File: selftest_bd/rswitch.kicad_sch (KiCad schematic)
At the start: 105 parts, among them K1 TQ2-5_Split, K10 TQ2-5_Split, K11 TQ2-5_Split, K12 TQ2-5_Split, K13 TQ2-5_Split, K14 TQ2-5_Split, K15 TQ2-5_Split, K16 TQ2-5_Split, K17 TQ2-5_Split, K2 TQ2-5_Split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

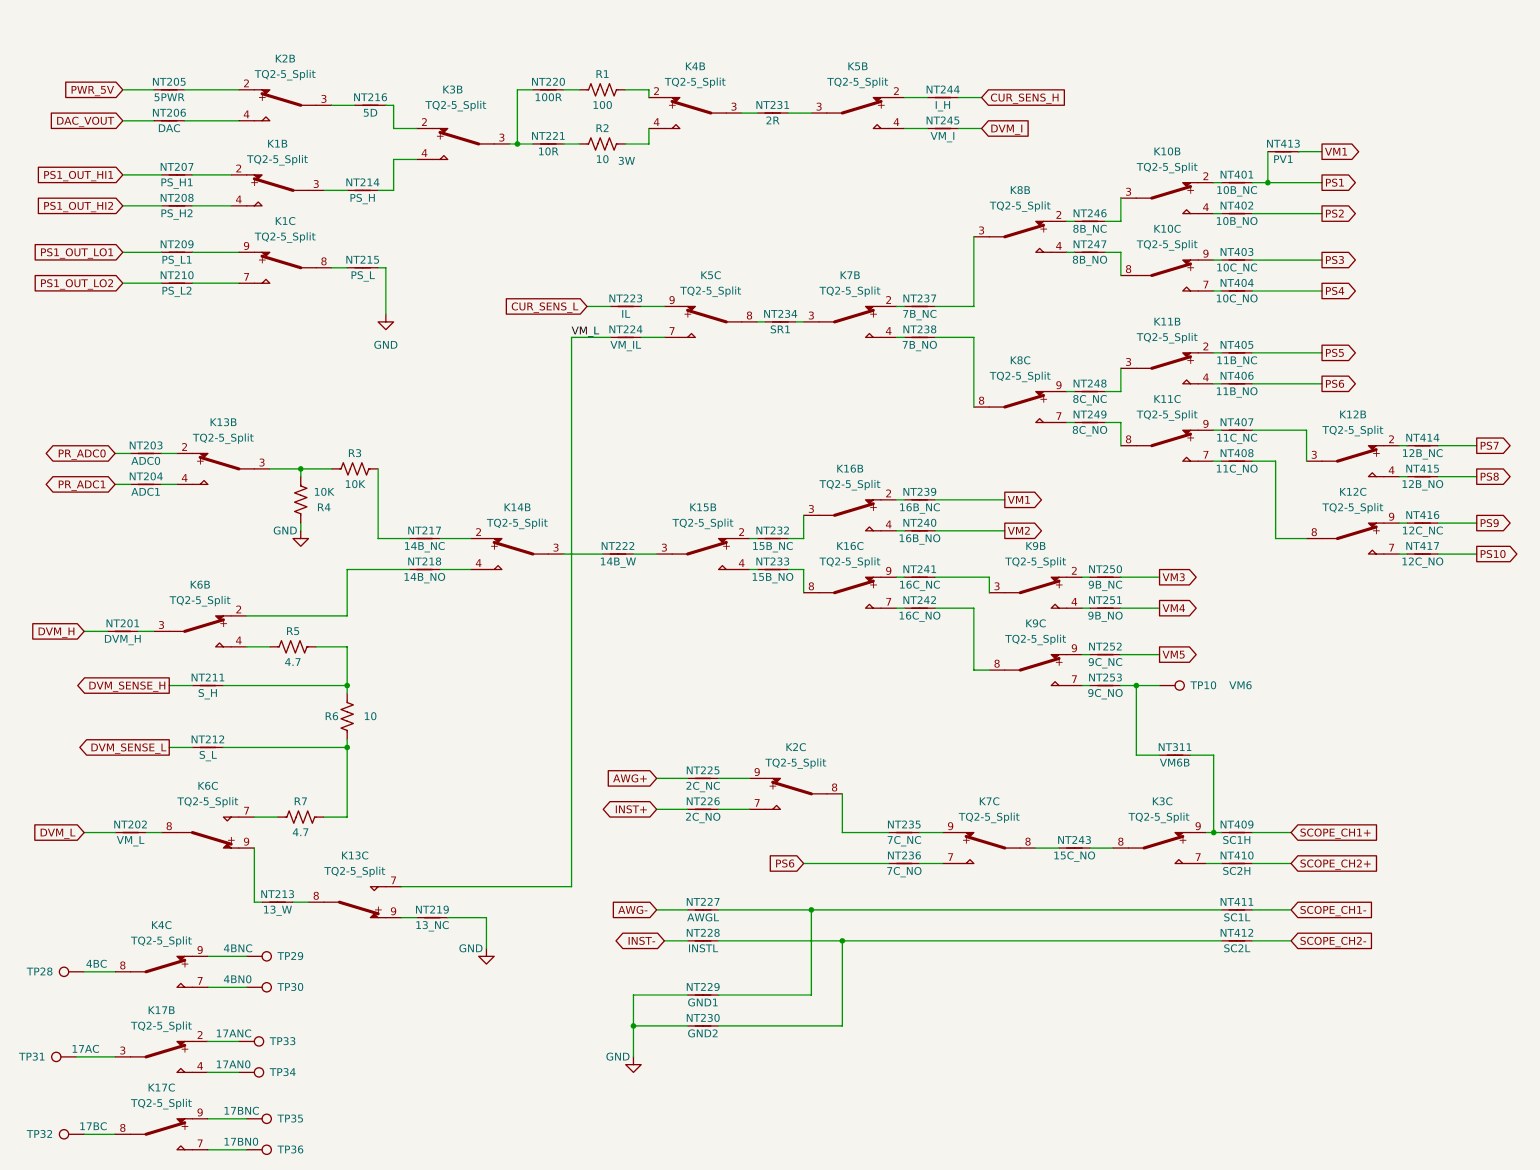
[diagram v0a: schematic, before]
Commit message: Commit V2.0
Redo PCB due to incorrect position of J1 and J2
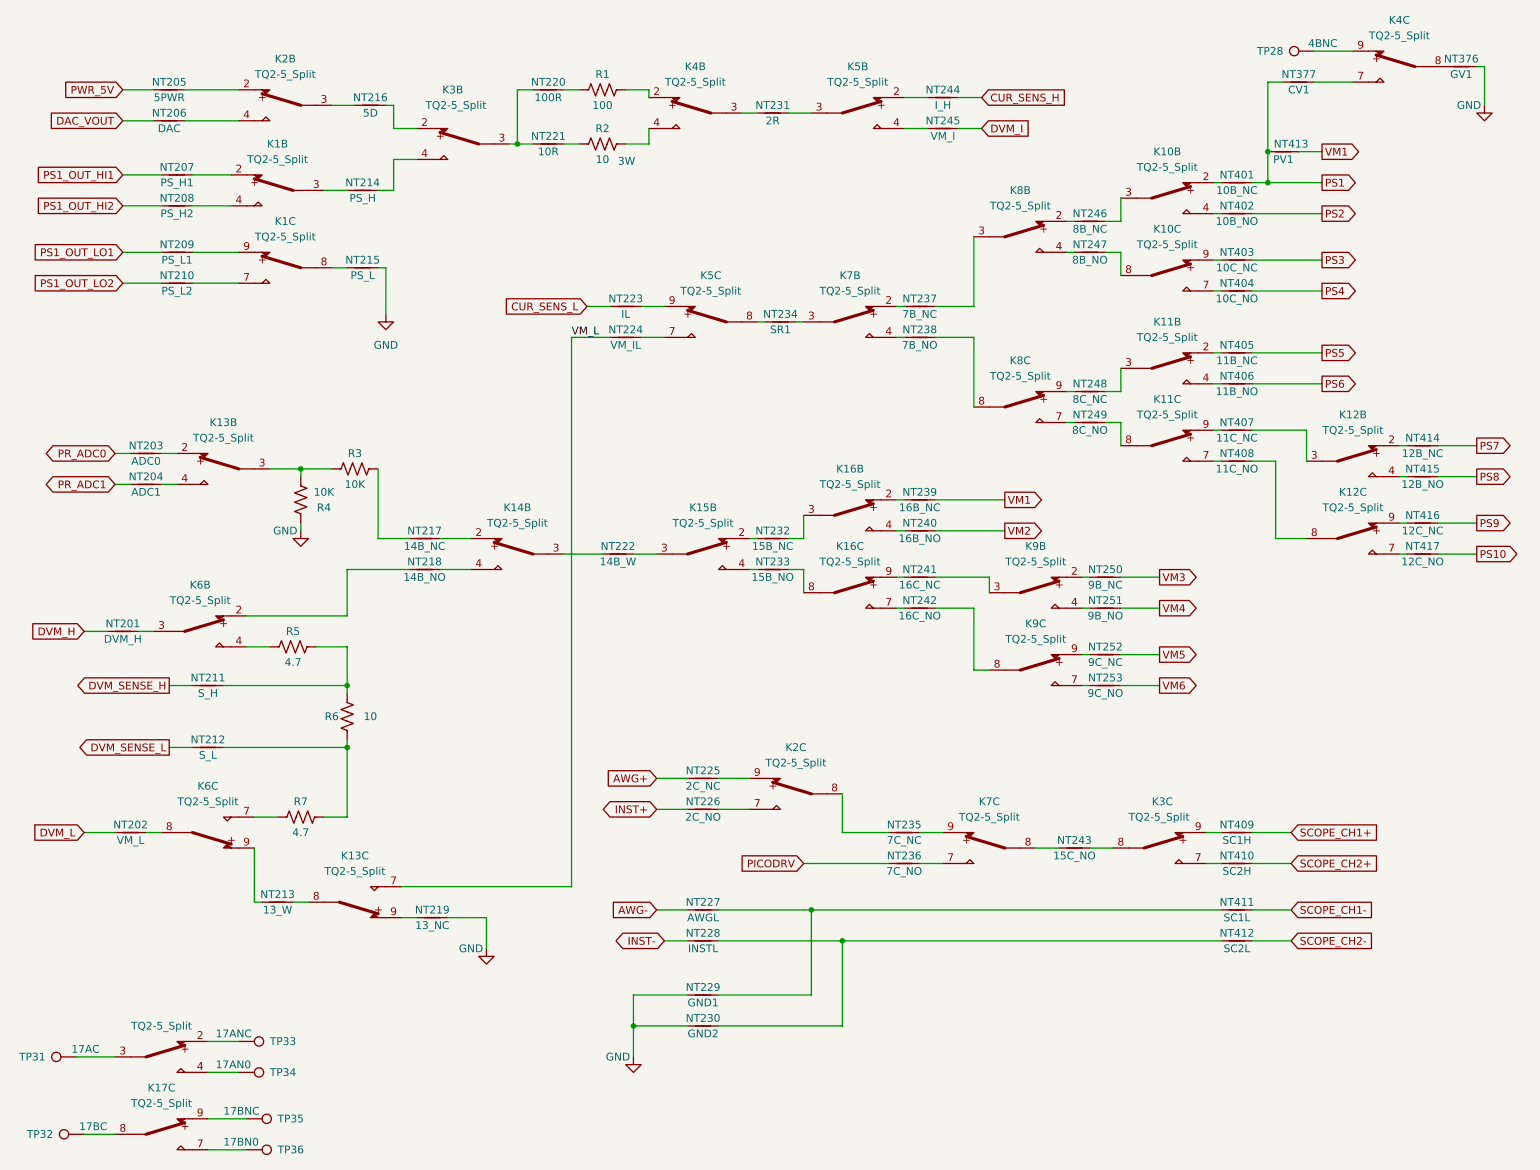
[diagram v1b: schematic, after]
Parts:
- removed NT311: VM6B, NetTie:NetTie-2_Front1.0mm, symbol Library:NetTie_2
- removed TP10: VM6, TestPoint:TestPoint_THTPad_D1.5mm_Drill0.7mm, symbol Library:TestPoint
- removed TP29: 4BNC, TestPoint:TestPoint_THTPad_D1.5mm_Drill0.7mm, symbol Library:TestPoint
- removed TP30: 4BN0, TestPoint:TestPoint_THTPad_D1.5mm_Drill0.7mm, symbol Library:TestPoint
- added NT376: GV1, NetTie:NetTie-2_Front1.0mm, symbol Library:NetTie_2
- added NT377: CV1, NetTie:NetTie-2_Front1.0mm, symbol Library:NetTie_2
- TP28: value 4BC -> 4BNC
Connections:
- net GND: now also NT376.2
- net PS1: now also NT377.1
- net PS6: no longer NT236.1
- net at K4.7: now also NT377.2
- net at K4.8: now also NT376.1; no longer TP28.1
- net at K4.9: now also TP28.1
- net VM6: now reaches NT253.2
- new net PICODRV: NT236.1
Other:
- title: FIRST TEST STATION SELFTEST BOARD 640-1010-010 -> FIRST TEST STATION SELFTEST BOARD 640-1010-020

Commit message: update README and small correction
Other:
- title: FIRST TEST STATION SELFTEST BOARD 640-1010-020 -> FIRST TEST STATION SELFTEST BOARD 640-1010-021
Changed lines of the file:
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@@
   (paper "A")
   (title_block
-    (title "FIRST TEST STATION SELFTEST BOARD 640-1010-020")
+    (title "FIRST TEST STATION SELFTEST BOARD 640-1010-021")
     (date "2023-10-01")
-    (rev "2.0")
+    (rev "2.1")
   )
   (junction (at 218.44 38.1) (diameter 0) (color 0 0 0 0)
